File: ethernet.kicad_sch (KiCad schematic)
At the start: 62 parts, among them J6 Bus_RJ45_5-2337992-8, U15 KSZ9031RNXCA, Y2 Oscillator_SMD_25MHz_KX-7

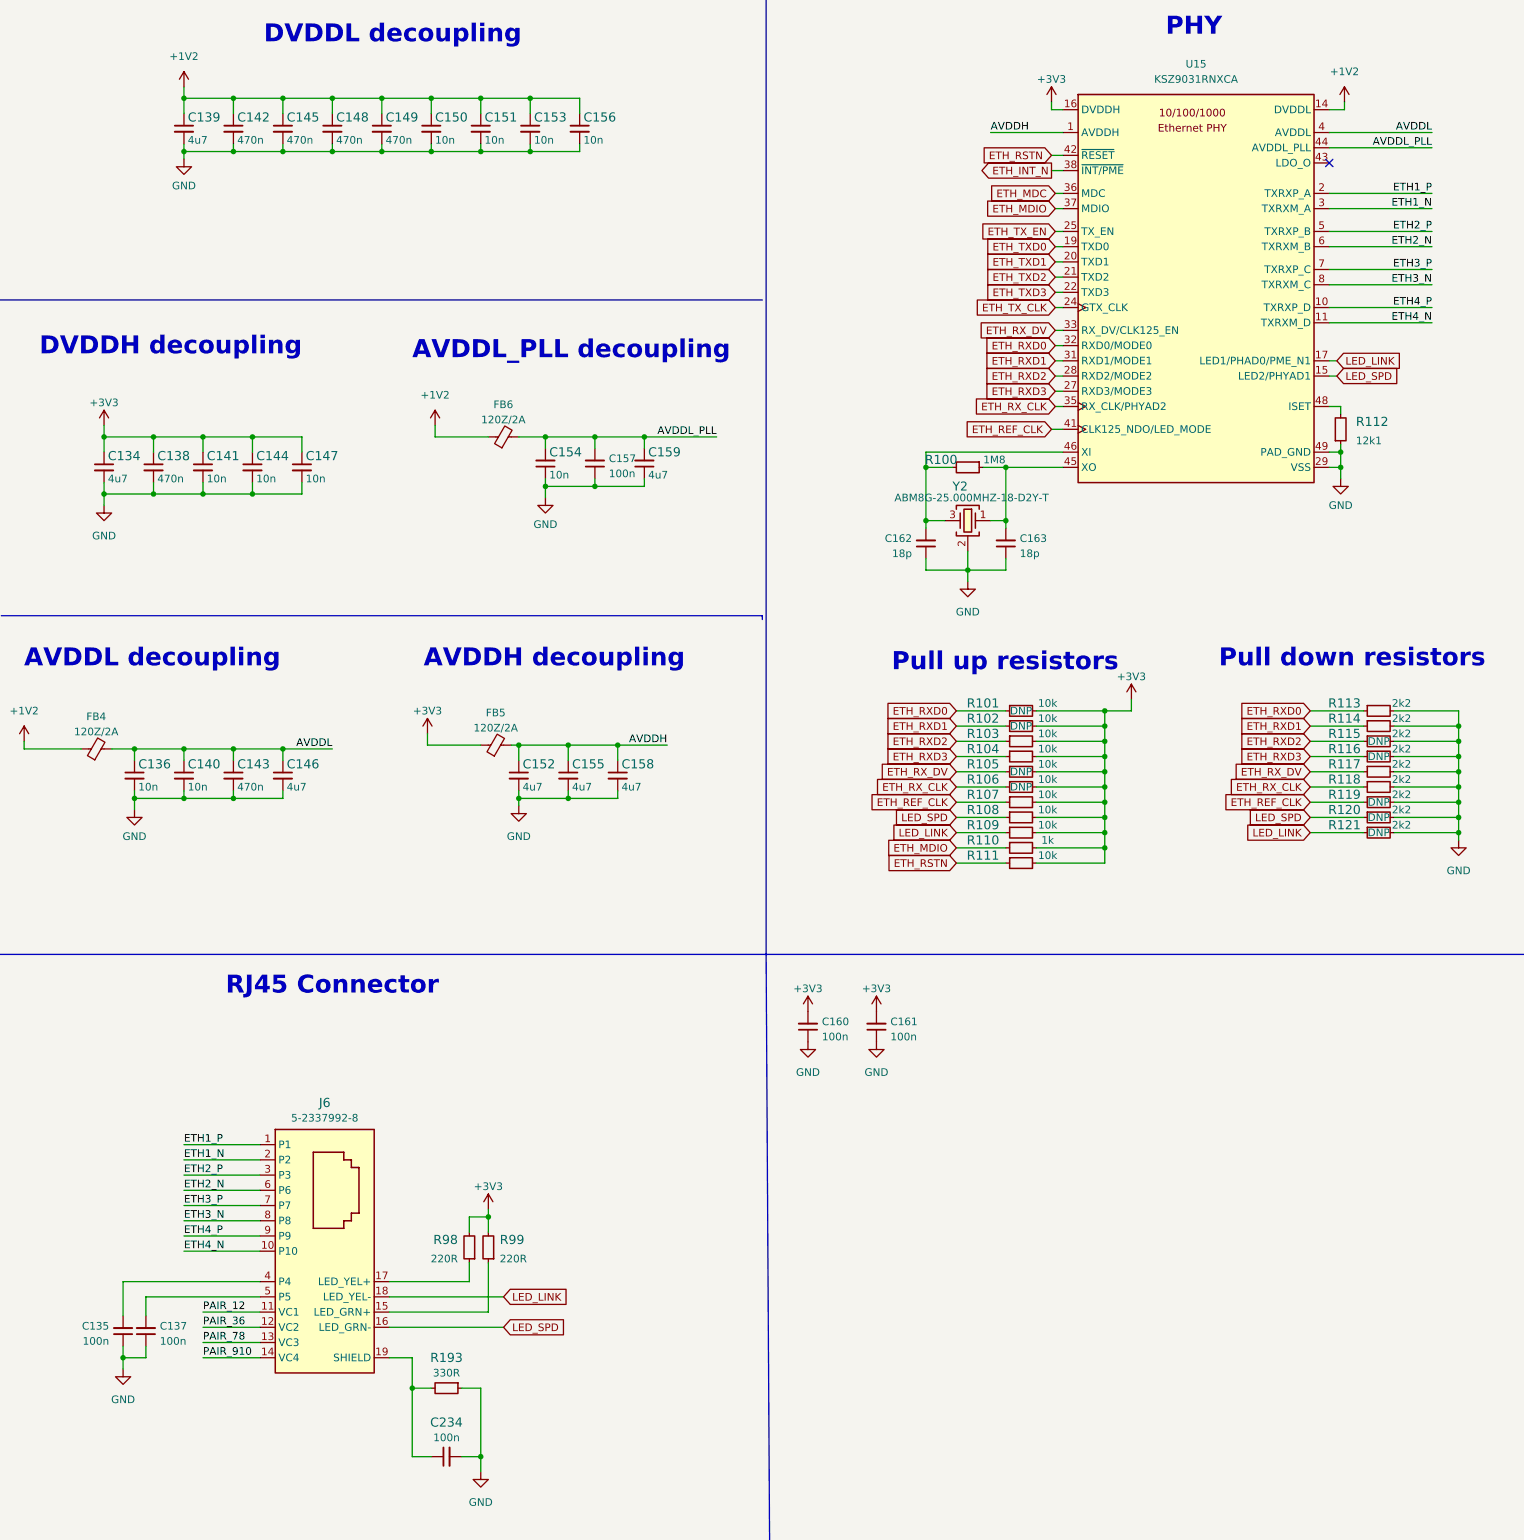
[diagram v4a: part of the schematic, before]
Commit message: Connect DDR hierarchical labels. Define and connect JTAG, RGMII, TDMS, UART, and SDIO buses. Reorganize schematic blocks between sheets
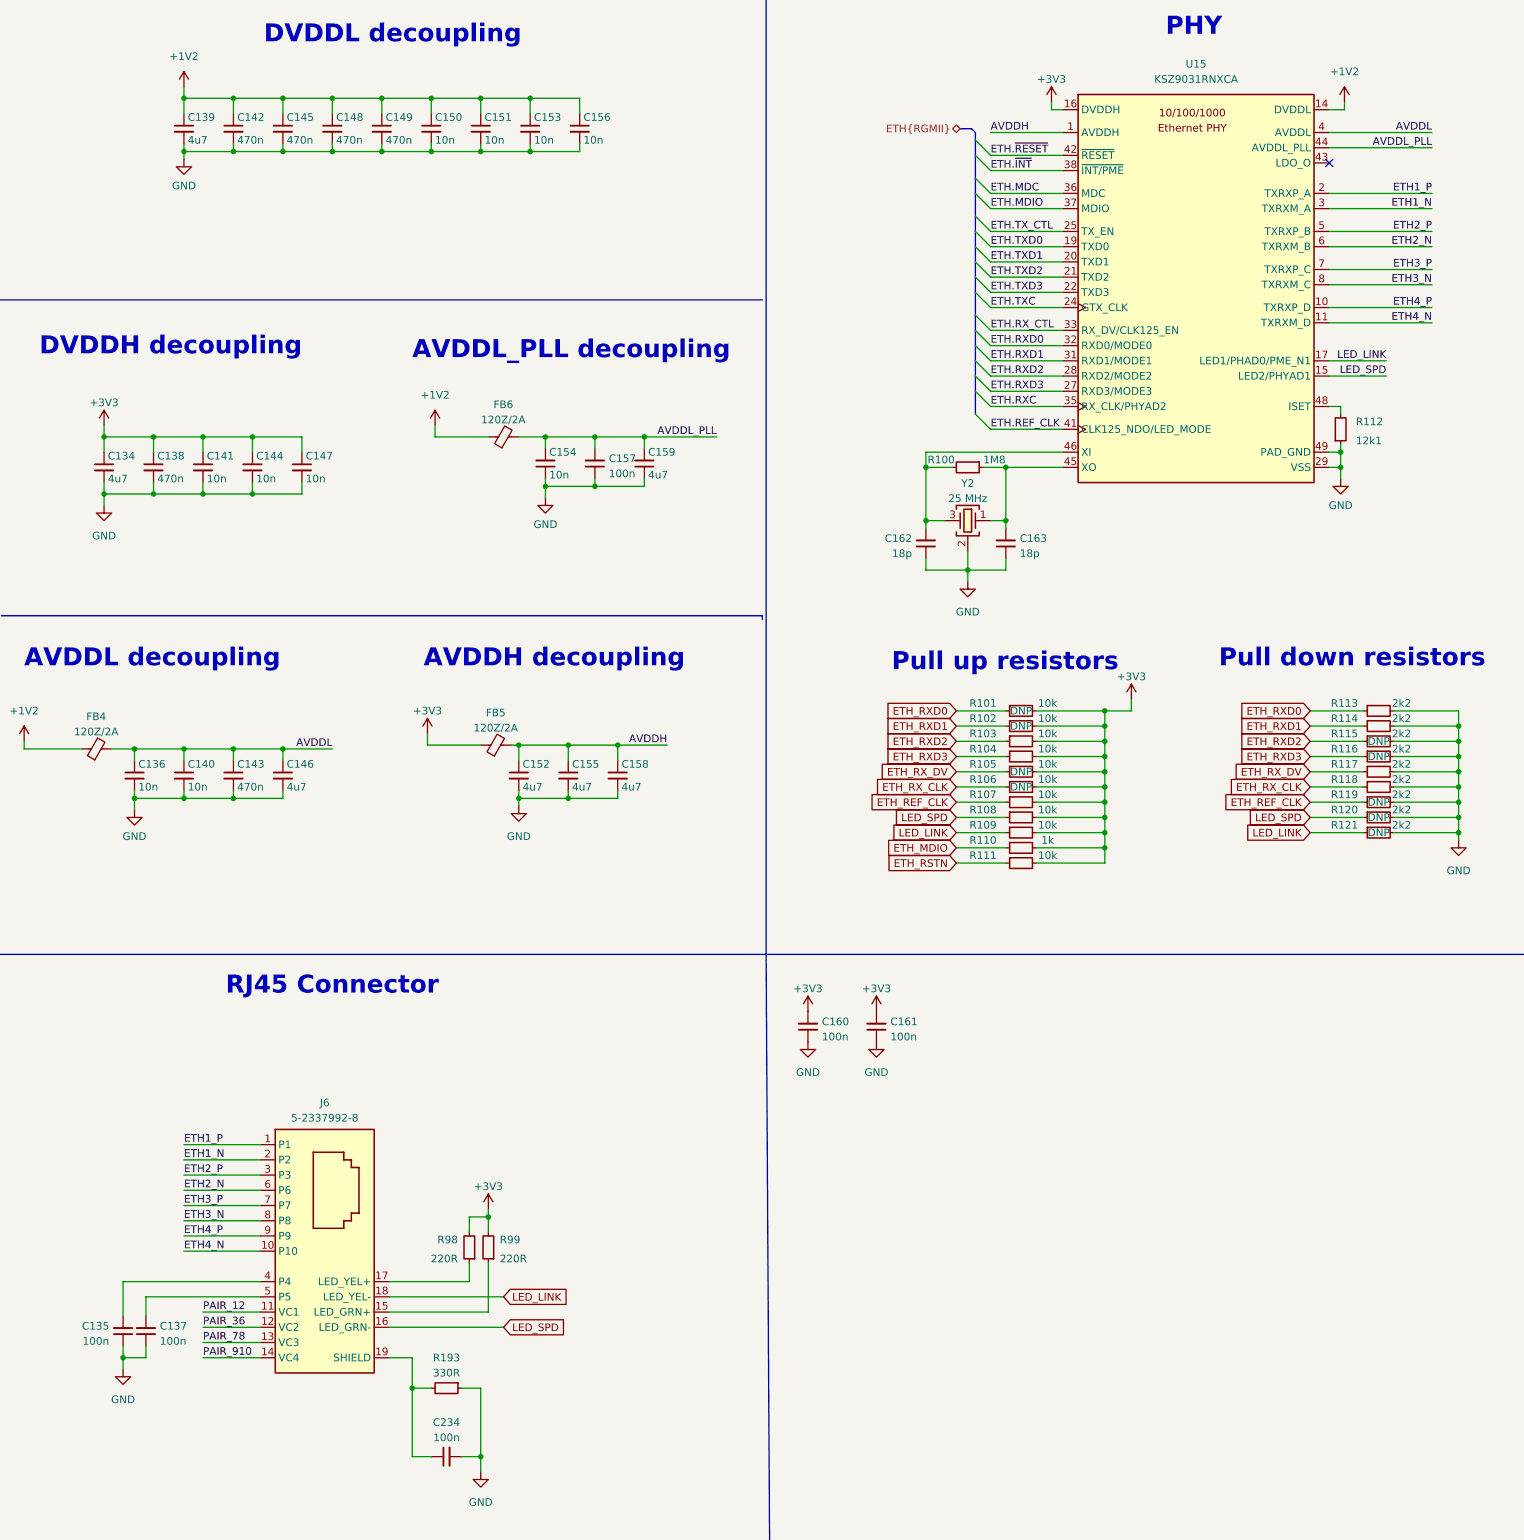
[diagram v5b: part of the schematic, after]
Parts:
- removed Y2: Oscillator_SMD_25MHz_KX-7, sodimm-ddr5-tester-footprints:Oscillator_SMD_Geyer_KX-7-4Pin_3.2x2.5mm, symbol sodimm-ddr5-tester:Oscillator_SMD_25MHz_KX-7
- added Y2: Resonator_25MHz_ABM8G, antmicro-footprints:Oscillator_SMD_Geyer_KX-7-4Pin_3.2x2.5mm, symbol antmicroResonators:Resonator_25MHz_ABM8G
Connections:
- net ETH_MDIO: no longer U15.37 (MDIO)
- net ETH_REF_CLK: no longer U15.41 (CLK125_NDO/LED_MODE)
- net ETH_RSTN: no longer U15.42 (~{RESET})
- net ETH_RXD0: no longer U15.32 (RXD0/MODE0)
- net ETH_RXD1: no longer U15.31 (RXD1/MODE1)
- net ETH_RXD2: no longer U15.28 (RXD2/MODE2)
- net ETH_RXD3: no longer U15.27 (RXD3/MODE3)
- net ETH_RX_CLK: no longer U15.35 (RX_CLK/PHYAD2)
- net ETH_RX_DV: no longer U15.33 (RX_DV/CLK125_EN)
- net GND: now also Y2.2 (SH), Y2.4 (SH)
- net at C163.2, R100.1, U15.45 (XO): now also Y2.1
- net at C162.2, R100.2, U15.46 (XI): now also Y2.3
- net ETH_INT_N renamed ETH.~{INT}
- net ETH_MDC renamed ETH.MDC
- net ETH_TXD0 renamed ETH.TXD0
- net ETH_TXD1 renamed ETH.TXD1
- net ETH_TXD2 renamed ETH.TXD2
- net ETH_TXD3 renamed ETH.TXD3
- net ETH_TX_CLK renamed ETH.TXC
- net ETH_TX_EN renamed ETH.TX_CTL
- new net ETH.MDIO: U15.37 (MDIO)
- new net ETH.REF_CLK: U15.41 (CLK125_NDO/LED_MODE)
- new net ETH.RXC: U15.35 (RX_CLK/PHYAD2)
- new net ETH.RXD0: U15.32 (RXD0/MODE0)
- new net ETH.RXD1: U15.31 (RXD1/MODE1)
- new net ETH.RXD2: U15.28 (RXD2/MODE2)
- new net ETH.RXD3: U15.27 (RXD3/MODE3)
- new net ETH.RX_CTL: U15.33 (RX_DV/CLK125_EN)
- new net ETH.~{RESET}: U15.42 (~{RESET})

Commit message: Finish creating hierarchical buses and structure, start reconnecting signals
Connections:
- net ETH_MDIO is gone; now on net ETH.MDIO: R110.1
- net ETH_REF_CLK is gone; now on net ETH.REF_CLK: R107.1, R119.1
- net ETH_RSTN is gone; now on net ETH.~{RESET}: R111.1
- net ETH_RXD0 is gone; now on net ETH.RXD0: R101.1, R113.1
- net ETH_RXD1 is gone; now on net ETH.RXD1: R102.1, R114.1
- net ETH_RXD2 is gone; now on net ETH.RXD2: R103.1, R115.1
- net ETH_RXD3 is gone; now on net ETH.RXD3: R104.1, R116.1
- net ETH_RX_CLK is gone; now on net ETH.RXC: R106.1, R118.1
- net ETH_RX_DV is gone; now on net ETH.RX_CTL: R105.1, R117.1
- net PAIR_12: no longer names the net of J6.11 (VC1)
- net PAIR_36: no longer names the net of J6.12 (VC2)
- net PAIR_78: no longer names the net of J6.13 (VC3)
- net PAIR_910: no longer names the net of J6.14 (VC4)
- no-connect marks 1 -> 5
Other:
- note added: "Bootstrap configuration"
- note added: "CLK125_EN"
- note added: "Gigabit Ethernet"
- note added: "LED_MODE"
- note added: "MODE0"
- note added: "MODE1"
- note added: "MODE2"
- note added: "MODE3"
- note added: "MODE[3:0] : 1100 (RGMII mode - Advertise 1000BASE-T full-duplex only) PHYAD[4:0]: 00011 CLK125_EN: 0, disabled LED_MODE: 1, Single-LED mode"
- note added: "PHYAD0"
- note added: "PHYAD1"
- note added: "PHYAD2"
- note added: "Reference plane decoupling"
- note removed: "AVDDH decoupling"
- note removed: "AVDDL decoupling"
- note removed: "AVDDL_PLL decoupling"
- note removed: "DVDDH decoupling"
- note removed: "DVDDL decoupling"
- note removed: "PHY"
- note removed: "Pull down resistors"
- note removed: "Pull up resistors"
- note removed: "RJ45 Connector"
- moved on the sheet: C134, C135, C136, C137, C138, C139, C140, C141, C142, C143, C144, C145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

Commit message: Loclib of the project
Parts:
- Y2: footprint antmicro-footprints:Oscillator_SMD_Geyer_KX-7-4Pin_3.2x2.5mm -> sodimm-ddr5-tester-footprints:Oscillator_SMD_Geyer_KX-7-4Pin_3.2x2.5mm; symbol antmicroResonators:Resonator_25MHz_ABM8G -> sodimm-ddr5-tester:Resonator_25MHz_ABM8G
